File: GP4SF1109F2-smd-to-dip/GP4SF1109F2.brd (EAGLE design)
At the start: 27.6 x 12.7 mm, 3 parts

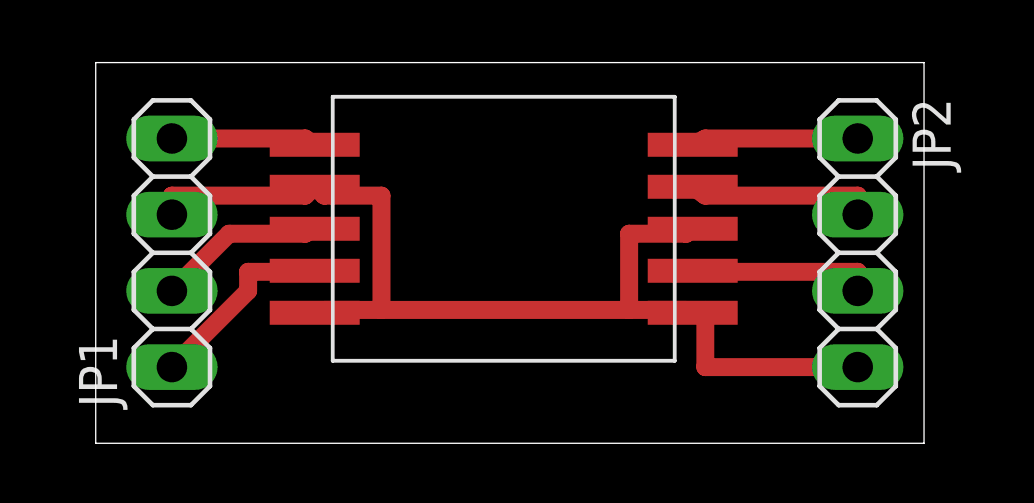
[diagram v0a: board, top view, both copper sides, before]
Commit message: GP4SF1109F2-smd-to-dip updated
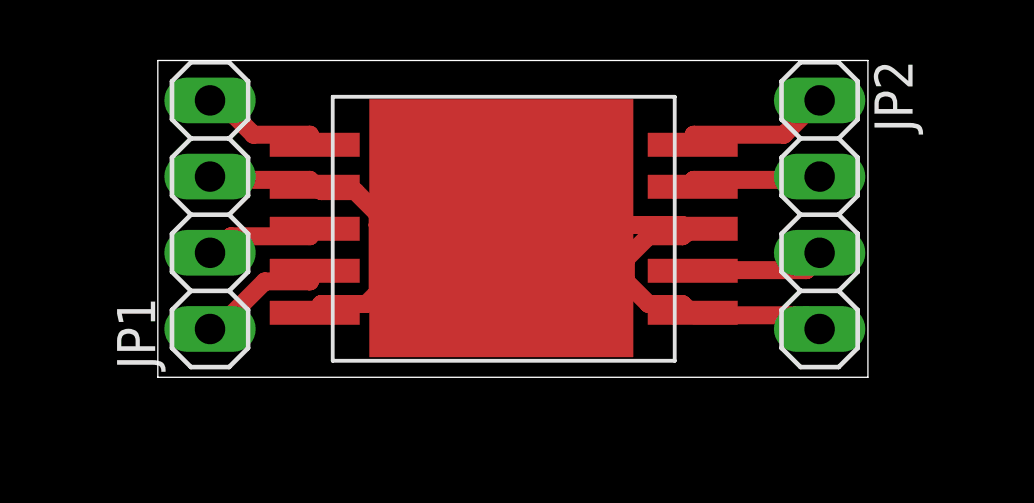
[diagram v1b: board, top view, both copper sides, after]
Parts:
- moved JP2 1.80 mm to (54.6, 57.1)
- moved JP1 1.80 mm to (34.3, 57.1)
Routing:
- net N$2: track 36.4 -> 32.1 mm
- net N$4: track 6.45 -> 4.35 mm
- net N$3: track 5.59 -> 3.83 mm
- net N$6: track 6.23 -> 4.50 mm
- net N$7: track 6.14 -> 4.54 mm
- net N$1: track 4.82 -> 4.17 mm
- net N$5: track 5.55 -> 5.01 mm
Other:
- board size 27.6 x 12.7 mm -> 23.7 x 10.6 mm
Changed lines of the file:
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@@
 <setting verticaltext="up"/>
 </settings>
-<grid distance="50" unitdist="mil" unit="mil" style="lines" multiple="1" display="no" altdistance="5" altunitdist="mil" altunit="mil"/>
+<grid distance="0.2" unitdist="mm" unit="mm" style="lines" multiple="1" display="no" altdistance="5" altunitdist="mil" altunit="mil"/>
 <layers>
 <layer number="1" name="Top" color="4" fill="1" visible="yes" active="yes"/>
@@
 <board>
 <plain>
-<wire x1="30.48" y1="49.53" x2="58.09" y2="49.53" width="0" layer="20"/>
-<wire x1="58.09" y1="49.53" x2="58.09" y2="62.22" width="0" layer="20"/>
-<wire x1="58.09" y1="62.22" x2="30.48" y2="62.22" width="0" layer="20"/>
-<wire x1="30.48" y1="62.22" x2="30.48" y2="49.53" width="0" layer="20"/>
+<wire x1="32.55" y1="51.73" x2="56.22" y2="51.73" width="0" layer="20"/>
+<wire x1="56.22" y1="51.73" x2="56.22" y2="62.29" width="0" layer="20"/>
+<wire x1="56.22" y1="62.29" x2="32.55" y2="62.29" width="0" layer="20"/>
+<wire x1="32.55" y1="62.29" x2="32.55" y2="51.73" width="0" layer="20"/>
+<rectangle x1="39.6" y1="52.4" x2="48.4" y2="61" layer="1"/>
 </plain>
 <attributes>
@@
 <autorouter>
 <pass name="Default">
-<param name="RoutingGrid" value="50mil"/>
+<param name="RoutingGrid" value="6.25mil"/>
 <param name="AutoGrid" value="1"/>
 <param name="Efforts" value="2"/>
@@
 </autorouter>
 <elements>
-<element name="JP1" library="pinhead" library_urn="urn:adsk.eagle:library:325" package="1X04" package3d_urn="urn:adsk.eagle:package:22407/2" value="" x="33.02" y="55.88" rot="R90"/>
+<element name="JP1" library="pinhead" library_urn="urn:adsk.eagle:library:325" package="1X04" package3d_urn="urn:adsk.eagle:package:22407/2" value="" x="34.29" y="57.15" rot="R90"/>
 <element name="U$1" library="mgvc" package="GP4SF1109F2" value="GP4SF1109F2" x="43.18" y="55.88"/>
-<element name="JP2" library="pinhead" library_urn="urn:adsk.eagle:library:325" package="1X04" package3d_urn="urn:adsk.eagle:package:22407/2" value="" x="55.88" y="55.88" rot="R270"/>
+<element name="JP2" library="pinhead" library_urn="urn:adsk.eagle:library:325" package="1X04" package3d_urn="urn:adsk.eagle:package:22407/2" value="" x="54.61" y="57.15" rot="R270"/>
 </elements>
 <signals>
@@
 <contactref element="U$1" pad="VIN"/>
 <contactref element="JP1" pad="4"/>
-<wire x1="33.02" y1="59.69" x2="37.465" y2="59.69" width="0.6" layer="1"/>
-<wire x1="37.465" y1="59.69" x2="37.78" y2="59.48" width="0.6" layer="1"/>
+<wire x1="35.739" y1="59.8158" x2="37.62" y2="59.8158" width="0.6" layer="1"/>
+<wire x1="34.6104" y1="60.9444" x2="35.739" y2="59.8158" width="0.6" layer="1"/>
+<wire x1="37.62" y1="59.8158" x2="37.78" y2="59.48" width="0.6" layer="1"/>
+<wire x1="34.6104" y1="60.9444" x2="34.29" y2="60.96" width="0.6" layer="1"/>
 </signal>
 <signal name="N$2">
@@
 <contactref element="JP1" pad="3"/>
 <contactref element="JP2" pad="4"/>
-<wire x1="33.02" y1="57.785" x2="37.465" y2="57.785" width="0.6" layer="1"/>
-<wire x1="33.02" y1="57.15" x2="33.02" y2="57.785" width="0.6" layer="1"/>
-<wire x1="37.465" y1="57.785" x2="37.78" y2="58.08" width="0.6" layer="1"/>
-<wire x1="50.165" y1="53.975" x2="48.26" y2="53.975" width="0.6" layer="1"/>
-<wire x1="48.26" y1="53.975" x2="40.005" y2="53.975" width="0.6" layer="1"/>
-<wire x1="40.005" y1="53.975" x2="38.1" y2="53.975" width="0.6" layer="1"/>
-<wire x1="38.1" y1="53.975" x2="37.78" y2="53.88" width="0.6" layer="1"/>
-<wire x1="50.165" y1="53.975" x2="50.38" y2="53.88" width="0.6" layer="1"/>
-<wire x1="48.26" y1="56.515" x2="50.165" y2="56.515" width="0.6" layer="1"/>
-<wire x1="48.26" y1="53.975" x2="48.26" y2="56.515" width="0.6" layer="1"/>
-<wire x1="50.165" y1="56.515" x2="50.38" y2="56.68" width="0.6" layer="1"/>
-<wire x1="50.8" y1="52.07" x2="55.88" y2="52.07" width="0.6" layer="1"/>
-<wire x1="50.8" y1="53.975" x2="50.8" y2="52.07" width="0.6" layer="1"/>
-<wire x1="50.8" y1="53.975" x2="50.38" y2="53.88" width="0.6" layer="1"/>
-<wire x1="40.005" y1="57.785" x2="38.1" y2="57.785" width="0.6" layer="1"/>
-<wire x1="40.005" y1="53.975" x2="40.005" y2="57.785" width="0.6" layer="1"/>
-<wire x1="38.1" y1="57.785" x2="37.78" y2="58.08" width="0.6" layer="1"/>
+<wire x1="54.1728" y1="53.7966" x2="50.4108" y2="53.7966" width="0.6" layer="1"/>
+<wire x1="54.549" y1="53.4204" x2="54.1728" y2="53.7966" width="0.6" layer="1"/>
+<wire x1="50.4108" y1="53.7966" x2="50.38" y2="53.88" width="0.6" layer="1"/>
+<wire x1="54.549" y1="53.4204" x2="54.61" y2="53.34" width="0.6" layer="1"/>
+<wire x1="48.906" y1="56.43" x2="50.0346" y2="56.43" width="0.6" layer="1"/>
+<wire x1="48.1536" y1="55.6776" x2="48.906" y2="56.43" width="0.6" layer="1"/>
+<wire x1="48.1536" y1="54.9252" x2="48.1536" y2="55.6776" width="0.6" layer="1"/>
+<wire x1="48.906" y1="54.1728" x2="48.1536" y2="54.9252" width="0.6" layer="1"/>
+<wire x1="50.0346" y1="54.1728" x2="48.906" y2="54.1728" width="0.6" layer="1"/>
+<wire x1="50.0346" y1="56.43" x2="50.38" y2="56.68" width="0.6" layer="1"/>
+<wire x1="50.0346" y1="54.1728" x2="50.38" y2="53.88" width="0.6" layer="1"/>
+<wire x1="39.501" y1="54.1728" x2="37.9962" y2="54.1728" width="0.6" layer="1"/>
+<wire x1="39.8772" y1="54.549" x2="39.501" y2="54.1728" width="0.6" layer="1"/>
+<wire x1="39.8772" y1="57.1824" x2="39.8772" y2="56.8062" width="0.6" layer="1"/>
+<wire x1="39.8772" y1="56.8062" x2="39.8772" y2="54.549" width="0.6" layer="1"/>
+<wire x1="39.1248" y1="57.9348" x2="39.8772" y2="57.1824" width="0.6" layer="1"/>
+<wire x1="37.9962" y1="57.9348" x2="39.1248" y2="57.9348" width="0.6" layer="1"/>
+<wire x1="37.9962" y1="54.1728" x2="37.78" y2="53.88" width="0.6" layer="1"/>
+<wire x1="37.9962" y1="57.9348" x2="37.78" y2="58.08" width="0.6" layer="1"/>
+<wire x1="37.62" y1="58.311" x2="34.6104" y2="58.311" width="0.6" layer="1"/>
+<wire x1="34.6104" y1="58.311" x2="34.29" y2="58.42" width="0.6" layer="1"/>
+<wire x1="37.62" y1="58.311" x2="37.78" y2="58.08" width="0.6" layer="1"/>
+<wire x1="39.8772" y1="56.8062" x2="50.0346" y2="56.8062" width="0.6" layer="1"/>
+<wire x1="50.0346" y1="56.8062" x2="50.38" y2="56.68" width="0.6" layer="1"/>
 </signal>
 <signal name="N$3">
 <contactref element="U$1" pad="RXD"/>
 <contactref element="JP1" pad="2"/>
-<wire x1="34.925" y1="56.515" x2="37.465" y2="56.515" width="0.6" layer="1"/>
-<wire x1="33.02" y1="54.61" x2="34.925" y2="56.515" width="0.6" layer="1"/>
-<wire x1="37.465" y1="56.515" x2="37.78" y2="56.68" width="0.6" layer="1"/>
+<wire x1="34.9866" y1="56.43" x2="37.62" y2="56.43" width="0.6" layer="1"/>
+<wire x1="34.6104" y1="56.0538" x2="34.9866" y2="56.43" width="0.6" layer="1"/>
+<wire x1="37.62" y1="56.43" x2="37.78" y2="56.68" width="0.6" layer="1"/>
+<wire x1="34.6104" y1="56.0538" x2="34.29" y2="55.88" width="0.6" layer="1"/>
 </signal>
 <signal name="N$4">
 <contactref element="U$1" pad="TXD"/>
 <contactref element="JP1" pad="1"/>
-<wire x1="35.56" y1="55.245" x2="37.465" y2="55.245" width="0.6" layer="1"/>
-<wire x1="35.56" y1="54.61" x2="35.56" y2="55.245" width="0.6" layer="1"/>
-<wire x1="33.02" y1="52.07" x2="35.56" y2="54.61" width="0.6" layer="1"/>
-<wire x1="37.465" y1="55.245" x2="37.78" y2="55.28" width="0.6" layer="1"/>
+<wire x1="36.1152" y1="54.9252" x2="37.62" y2="54.9252" width="0.6" layer="1"/>
+<wire x1="34.6104" y1="53.4204" x2="36.1152" y2="54.9252" width="0.6" layer="1"/>
+<wire x1="37.62" y1="54.9252" x2="37.78" y2="55.28" width="0.6" layer="1"/>
+<wire x1="34.6104" y1="53.4204" x2="34.29" y2="53.34" width="0.6" layer="1"/>
 </signal>
 <signal name="N$5">
 <contactref element="U$1" pad="ON/OFF"/>
 <contactref element="JP2" pad="1"/>
-<wire x1="55.88" y1="59.69" x2="50.8" y2="59.69" width="0.6" layer="1"/>
-<wire x1="50.8" y1="59.69" x2="50.38" y2="59.48" width="0.6" layer="1"/>
+<wire x1="53.4204" y1="59.8158" x2="50.4108" y2="59.8158" width="0.6" layer="1"/>
+<wire x1="54.549" y1="60.9444" x2="53.4204" y2="59.8158" width="0.6" layer="1"/>
+<wire x1="50.4108" y1="59.8158" x2="50.38" y2="59.48" width="0.6" layer="1"/>
+<wire x1="54.549" y1="60.9444" x2="54.61" y2="60.96" width="0.6" layer="1"/>
 </signal>
 <signal name="N$6">
 <contactref element="U$1" pad="N/S"/>
 <contactref element="JP2" pad="2"/>
-<wire x1="55.88" y1="57.785" x2="50.8" y2="57.785" width="0.6" layer="1"/>
-<wire x1="55.88" y1="57.15" x2="55.88" y2="57.785" width="0.6" layer="1"/>
-<wire x1="50.8" y1="57.785" x2="50.38" y2="58.08" width="0.6" layer="1"/>
+<wire x1="54.549" y1="58.311" x2="50.4108" y2="58.311" width="0.6" layer="1"/>
+<wire x1="50.4108" y1="58.311" x2="50.38" y2="58.08" width="0.6" layer="1"/>
+<wire x1="54.549" y1="58.311" x2="54.61" y2="58.42" width="0.6" layer="1"/>
 </signal>
 <signal name="N$7">
 <contactref element="U$1" pad="RF_IN"/>
 <contactref element="JP2" pad="3"/>
-<wire x1="55.88" y1="55.245" x2="50.8" y2="55.245" width="0.6" layer="1"/>
-<wire x1="55.88" y1="54.61" x2="55.88" y2="55.245" width="0.6" layer="1"/>
-<wire x1="50.8" y1="55.245" x2="50.38" y2="55.28" width="0.6" layer="1"/>
+<wire x1="54.1728" y1="55.3014" x2="50.4108" y2="55.3014" width="0.6" layer="1"/>
+<wire x1="54.549" y1="55.6776" x2="54.1728" y2="55.3014" width="0.6" layer="1"/>
+<wire x1="50.4108" y1="55.3014" x2="50.38" y2="55.28" width="0.6" layer="1"/>
+<wire x1="54.549" y1="55.6776" x2="54.61" y2="55.88" width="0.6" layer="1"/>
 </signal>
 </signals>
